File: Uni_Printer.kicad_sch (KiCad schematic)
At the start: 9 parts, among them J5 FIDUCIAL, J6 FIDUCIAL

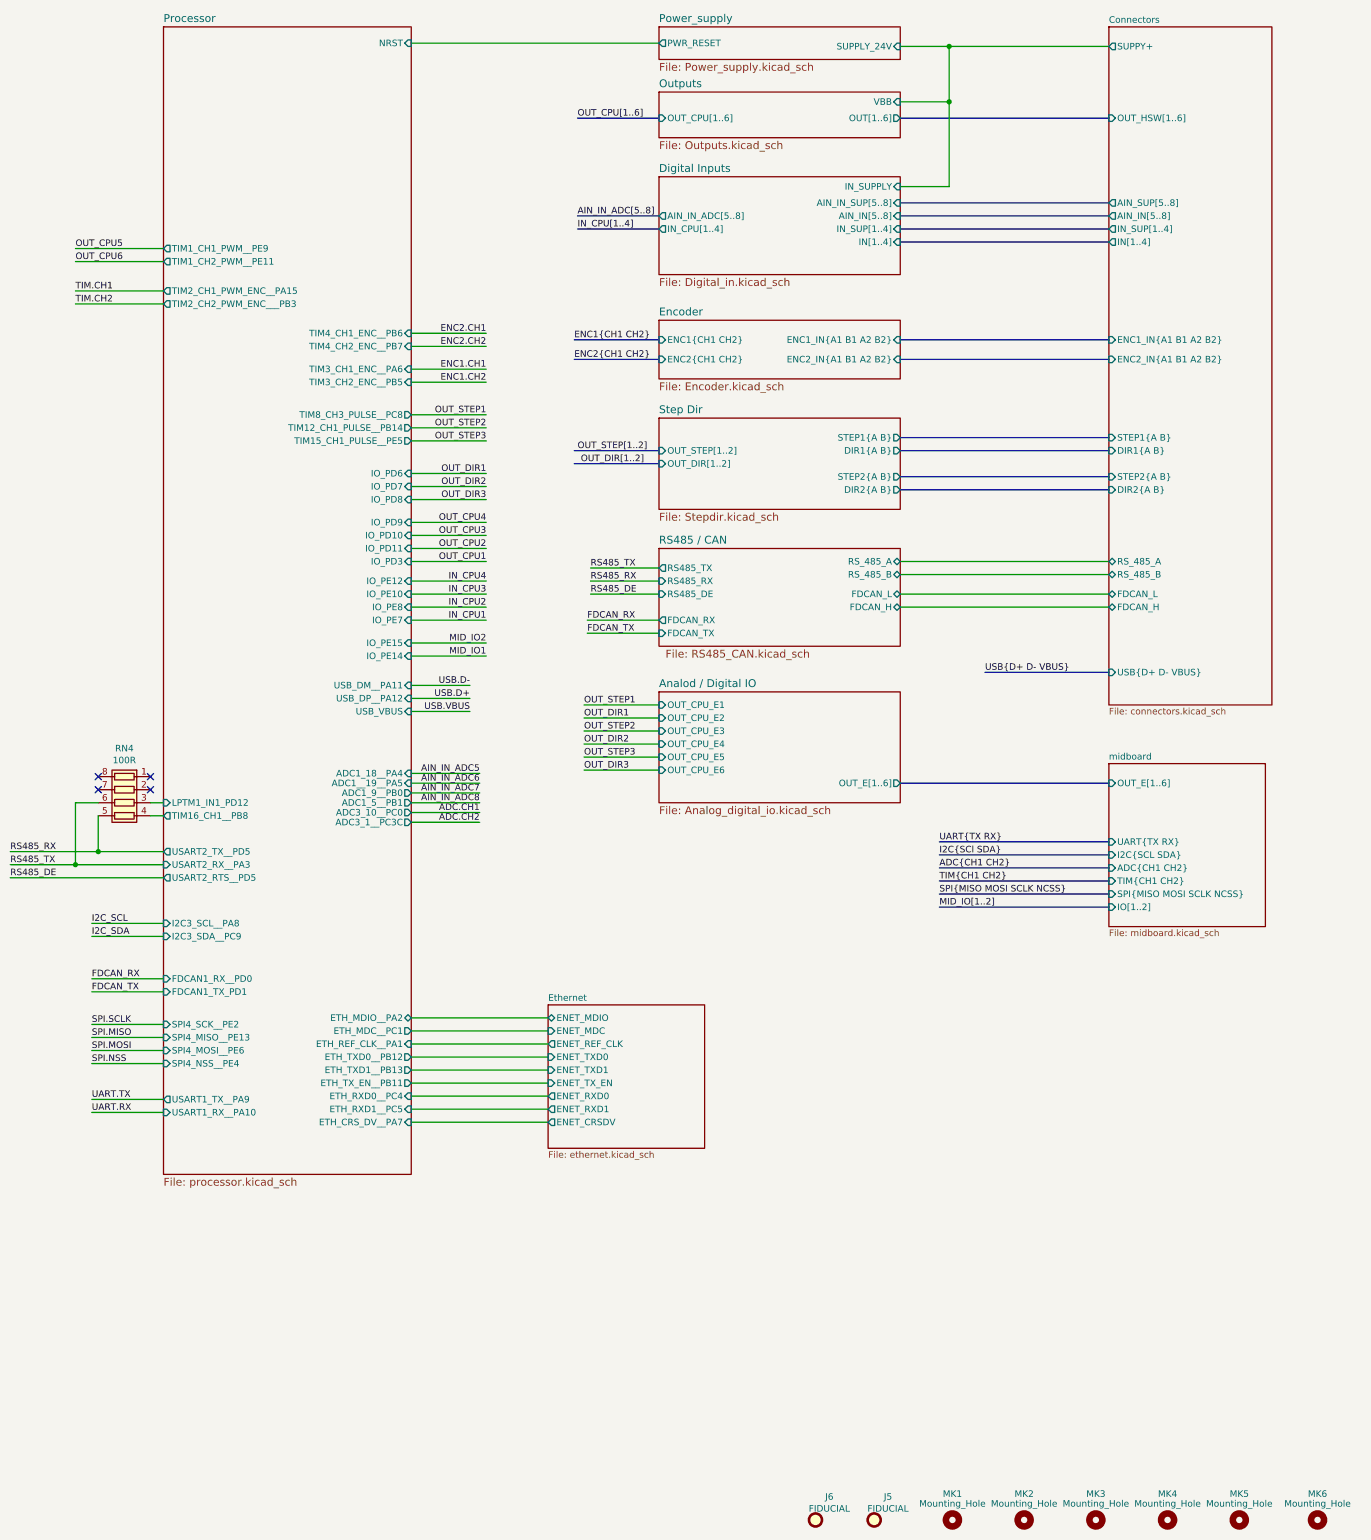
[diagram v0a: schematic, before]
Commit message: UPDATE - LAN chipset waiting for verification
Signed-off-by: Jacek <matuszewski.kartech@gmail.com>
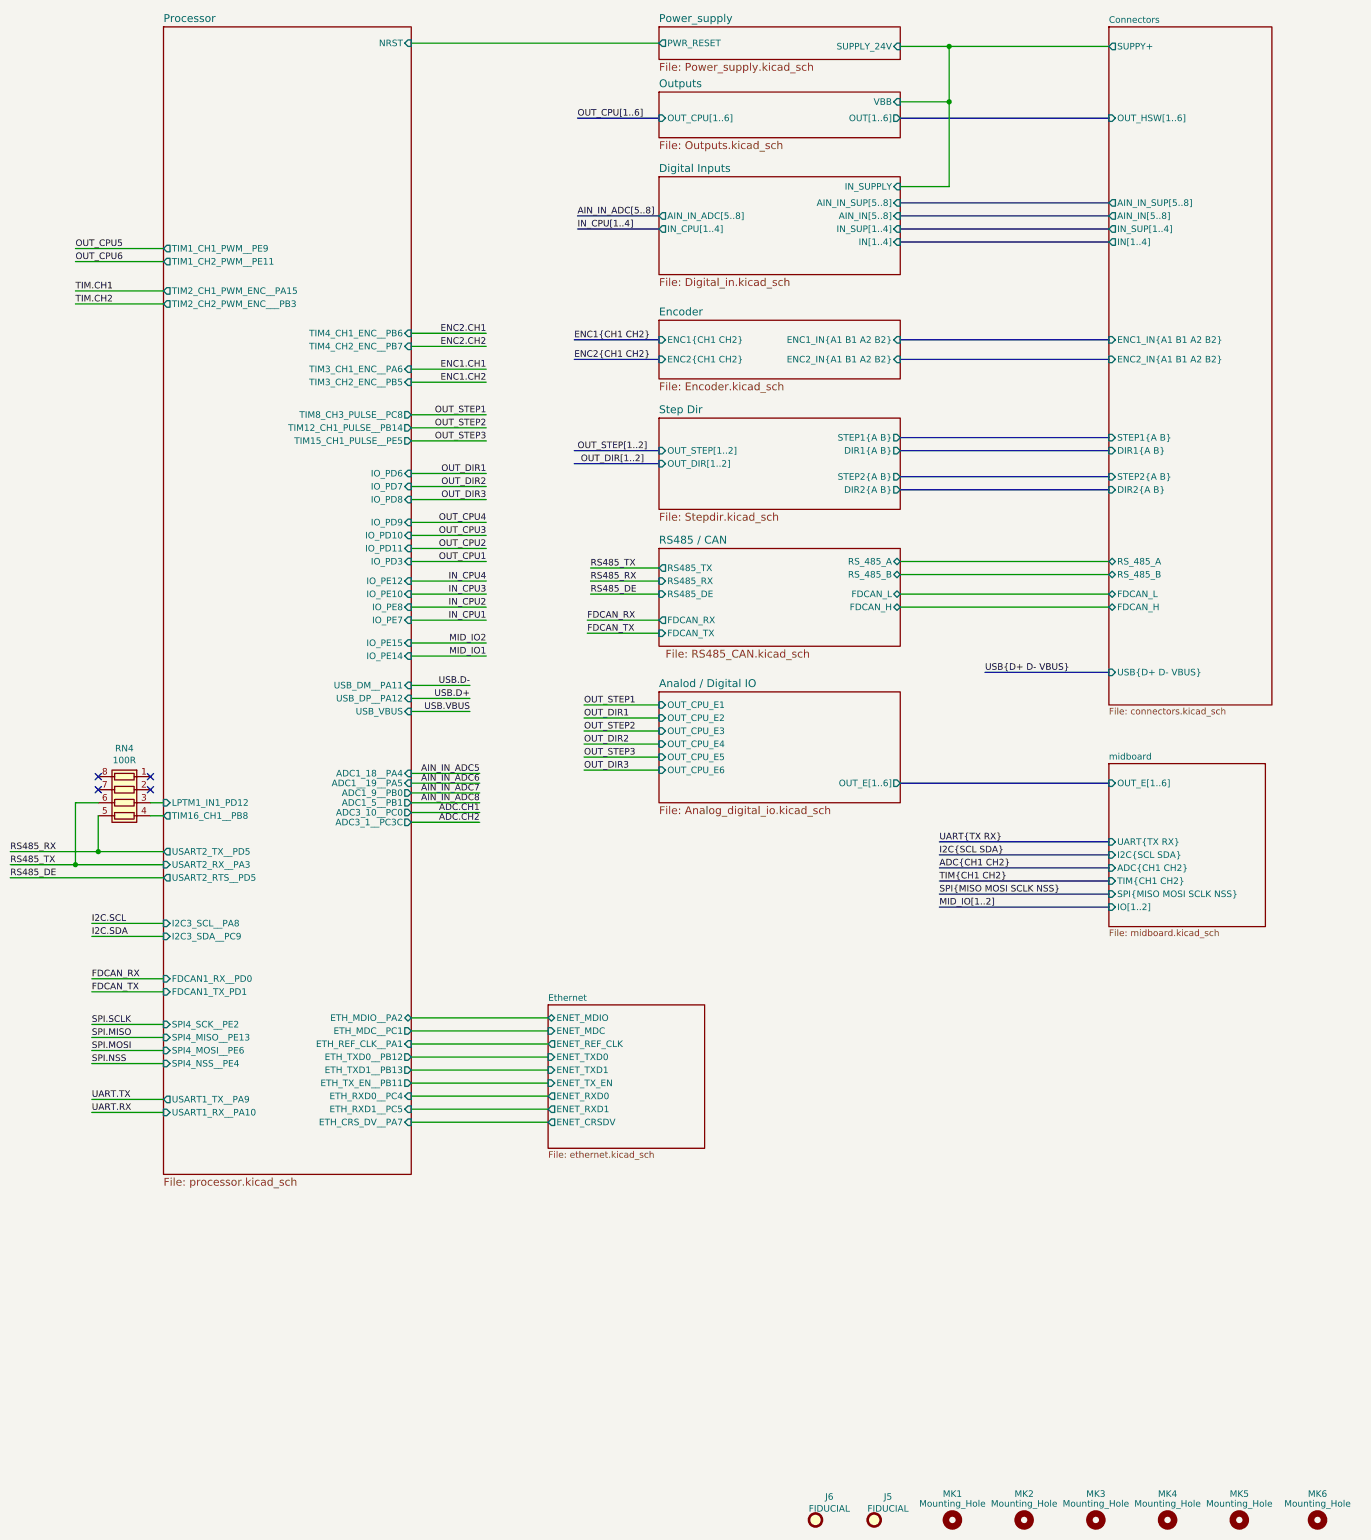
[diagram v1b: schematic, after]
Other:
- sheet Connectors ports: added AIN_IN_SUP[5..8]; removed AIN_SUP[5..8]
- sheet midboard ports: added SPI{MISO MOSI SCLK NSS}; removed SPI{MISO MOSI SCLK NCSS}
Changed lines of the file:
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@@
 (kicad_sch (version 20201015) (generator eeschema)
-  (page 1 12)
   (paper "A3" portrait)
   (title_block
@@
   (junction (at 202.565 82.55) (diameter 1.016) (color 0 0 0 0))
   (junction (at 202.565 93.345) (diameter 1.016) (color 0 0 0 0))
+  (no_connect (at 36.83 224.79))
   (no_connect (at 46.99 227.33))
-  (no_connect (at 36.83 224.79))
+  (no_connect (at 46.99 224.79))
   (no_connect (at 36.83 227.33))
-  (no_connect (at 46.99 224.79))
   (wire (pts (xy 19.685 239.395) (xy 36.83 239.395))
     (stroke (width 0) (type solid) (color 0 0 0 0))
@@
     (effects (font (size 1.27 1.27)) (justify left bottom))
   )
-  (label "I2C_SCL" (at 35.56 253.365 0)
-    (effects (font (size 1.27 1.27)) (justify left bottom))
-  )
-  (label "I2C_SDA" (at 35.56 255.905 0)
+  (label "I2C.SCL" (at 35.56 253.365 0)
+    (effects (font (size 1.27 1.27)) (justify left bottom))
+  )
+  (label "I2C.SDA" (at 35.56 255.905 0)
     (effects (font (size 1.27 1.27)) (justify left bottom))
   )
@@
     (effects (font (size 1.27 1.27)) (justify left bottom))
   )
-  (label "I2C{SCl SDA}" (at 200.66 240.03 0)
+  (label "I2C{SCL SDA}" (at 200.66 240.03 0)
     (effects (font (size 1.27 1.27)) (justify left bottom))
   )
@@
     (effects (font (size 1.27 1.27)) (justify left bottom))
   )
-  (label "SPI{MISO MOSI SCLK NCSS}" (at 200.66 247.65 0)
+  (label "SPI{MISO MOSI SCLK NSS}" (at 200.66 247.65 0)
     (effects (font (size 1.27 1.27)) (justify left bottom))
   )
@@
     (stroke (width 0) (type solid) (color 0 0 0 0))
     (fill (color 0 0 0 0.0000))
-    (property "Sheet name" "Analod / Digital IO" (id 0) (at 146.05 207.5175 0)
+    (property "Nazwa arkusza" "Analod / Digital IO" (id 0) (at 146.05 207.5175 0)
       (effects (font (size 1.524 1.524)) (justify left bottom))
     )
@@
     (stroke (width 0.001) (type solid) (color 132 0 132 1))
     (fill (color 255 255 255 0.0000))
-    (property "Sheet name" "Connectors" (id 0) (at 233.68 78.1041 0)
+    (property "Nazwa arkusza" "Connectors" (id 0) (at 233.68 78.1041 0)
       (effects (font (size 1.27 1.27)) (justify left bottom))
     )
@@
       (effects (font (size 1.27 1.27)) (justify left))
     )
-    (pin "AIN_SUP[5..8]" output (at 233.68 113.03 180)
+    (pin "AIN_IN_SUP[5..8]" output (at 233.68 113.03 180)
       (effects (font (size 1.27 1.27)) (justify left))
     )
@@
     (stroke (width 0) (type solid) (color 0 0 0 0))
     (fill (color 0 0 0 0.0000))
-    (property "Sheet name" "Digital Inputs" (id 0) (at 146.05 107.1875 0)
+    (property "Nazwa arkusza" "Digital Inputs" (id 0) (at 146.05 107.1875 0)
       (effects (font (size 1.524 1.524)) (justify left bottom))
     )
@@
     (stroke (width 0) (type solid) (color 0 0 0 0))
     (fill (color 0 0 0 0.0000))
-    (property "Sheet name" "Encoder" (id 0) (at 146.05 135.1275 0)
+    (property "Nazwa arkusza" "Encoder" (id 0) (at 146.05 135.1275 0)
       (effects (font (size 1.524 1.524)) (justify left bottom))
     )
@@
     (stroke (width 0) (type solid) (color 0 0 0 0))
     (fill (color 0 0 0 0.0000))
-    (property "Sheet name" "Ethernet" (id 0) (at 124.46 268.6045 0)
+    (property "Nazwa arkusza" "Ethernet" (id 0) (at 124.46 268.6045 0)
       (effects (font (size 1.27 1.27)) (justify left bottom))
     )
@@
     (stroke (width 0) (type solid) (color 0 0 0 0))
     (fill (color 0 0 0 0.0000))
-    (property "Sheet name" "Outputs" (id 0) (at 146.05 90.6775 0)
+    (property "Nazwa arkusza" "Outputs" (id 0) (at 146.05 90.6775 0)
       (effects (font (size 1.524 1.524)) (justify left bottom))
     )
@@
     (stroke (width 0) (type solid) (color 0 0 0 0))
     (fill (color 0 0 0 0.0000))
-    (property "Sheet name" "Power_supply" (id 0) (at 146.05 77.9775 0)
+    (property "Nazwa arkusza" "Power_supply" (id 0) (at 146.05 77.9775 0)
       (effects (font (size 1.524 1.524)) (justify left bottom))
     )
@@
     (stroke (width 0) (type solid) (color 0 0 0 0))
     (fill (color 0 0 0 0.0000))
-    (property "Sheet name" "Processor" (id 0) (at 49.53 77.9775 0)
+    (property "Nazwa arkusza" "Processor" (id 0) (at 49.53 77.9775 0)
       (effects (font (size 1.524 1.524)) (justify left bottom))
     )
@@
     (stroke (width 0) (type solid) (color 0 0 0 0))
     (fill (color 0 0 0 0.0000))
-    (property "Sheet name" "RS485 / CAN" (id 0) (at 146.05 179.5775 0)
+    (property "Nazwa arkusza" "RS485 / CAN" (id 0) (at 146.05 179.5775 0)
       (effects (font (size 1.524 1.524)) (justify left bottom))
     )
@@
     (stroke (width 0) (type solid) (color 0 0 0 0))
     (fill (color 0 0 0 0.0000))
-    (property "Sheet name" "Step Dir" (id 0) (at 146.05 154.1775 0)
+    (property "Nazwa arkusza" "Step Dir" (id 0) (at 146.05 154.1775 0)
       (effects (font (size 1.524 1.524)) (justify left bottom))
     )
@@
     (stroke (width 0.001) (type solid) (color 132 0 132 1))
     (fill (color 255 255 255 0.0000))
-    (property "Sheet name" "midboard" (id 0) (at 233.68 221.6141 0)
+    (property "Nazwa arkusza" "midboard" (id 0) (at 233.68 221.6141 0)
       (effects (font (size 1.27 1.27)) (justify left bottom))
     )
@@
       (effects (font (size 1.27 1.27)) (justify left))
     )
-    (pin "SPI{MISO MOSI SCLK NCSS}" input (at 233.68 247.65 180)
-      (effects (font (size 1.27 1.27)) (justify left))
-    )
+    (pin "SPI{MISO MOSI SCLK NSS}" input (at 233.68 247.65 180)
+      (effects (font (size 1.27 1.27)) (justify left))
+    )

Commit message: Fixes
Signed-off-by: Jarosław Karwik <jaroslaw.karwik@gmail.com>
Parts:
- RN4: TME DR1206-390K-4/8 -> DR1206-100R-4/8
